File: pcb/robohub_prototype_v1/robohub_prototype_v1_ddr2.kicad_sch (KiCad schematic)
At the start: 41 parts, among them U1 ATSAMA5D27C, U31 W972GG6KB-25, U32 W972GG6KB-25

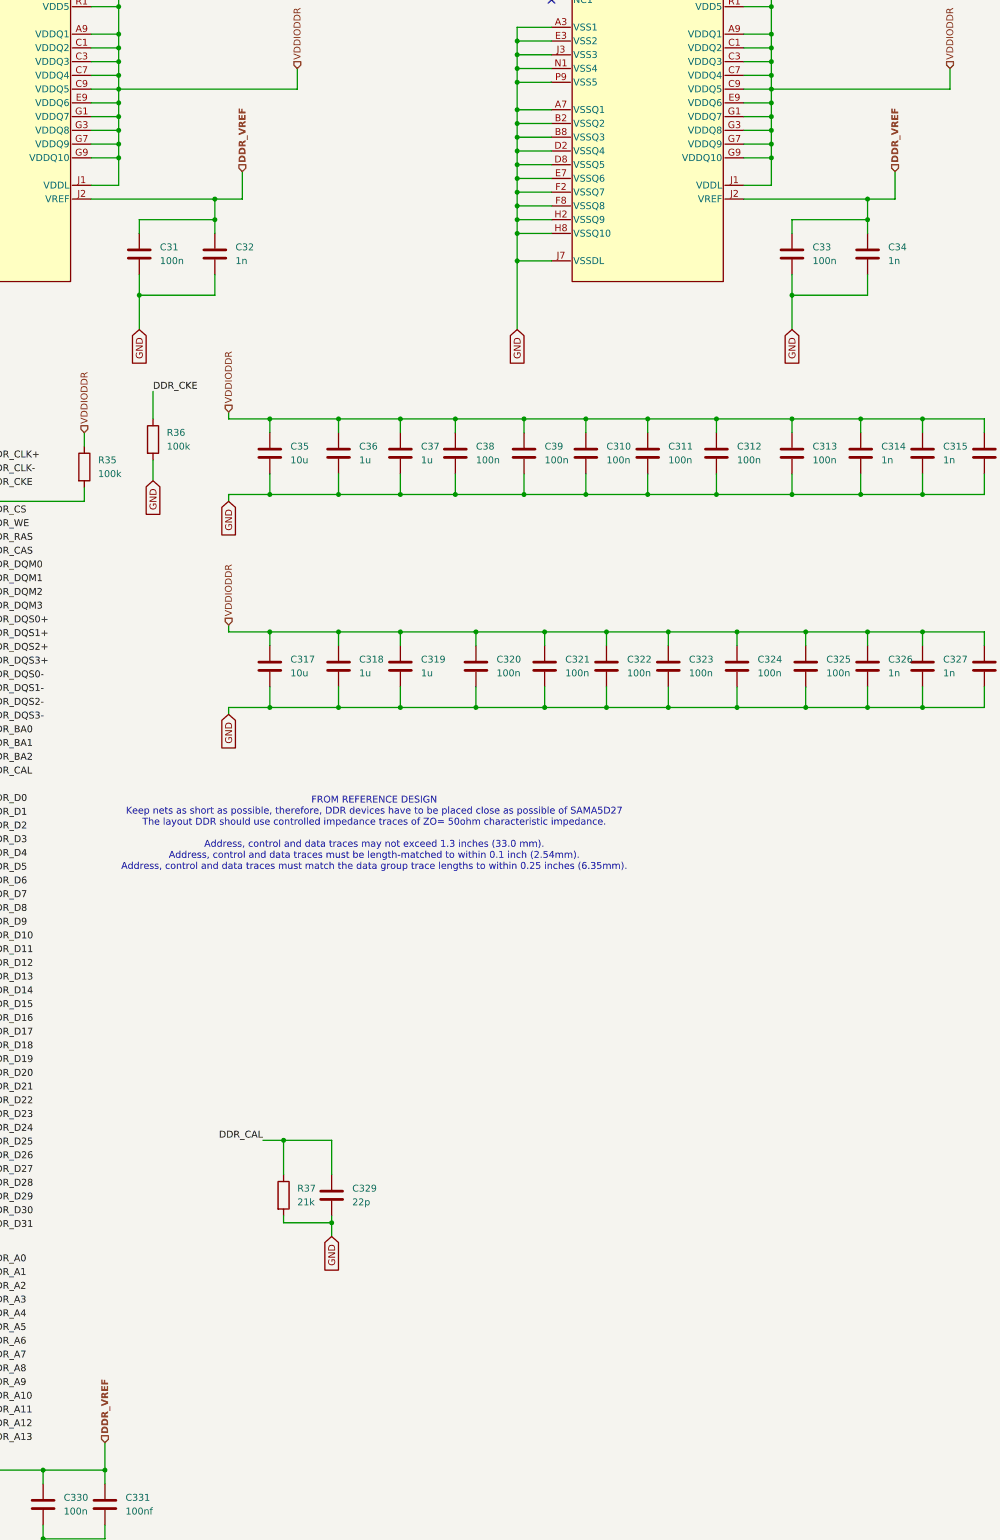
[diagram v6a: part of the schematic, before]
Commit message: Start routing ddr2
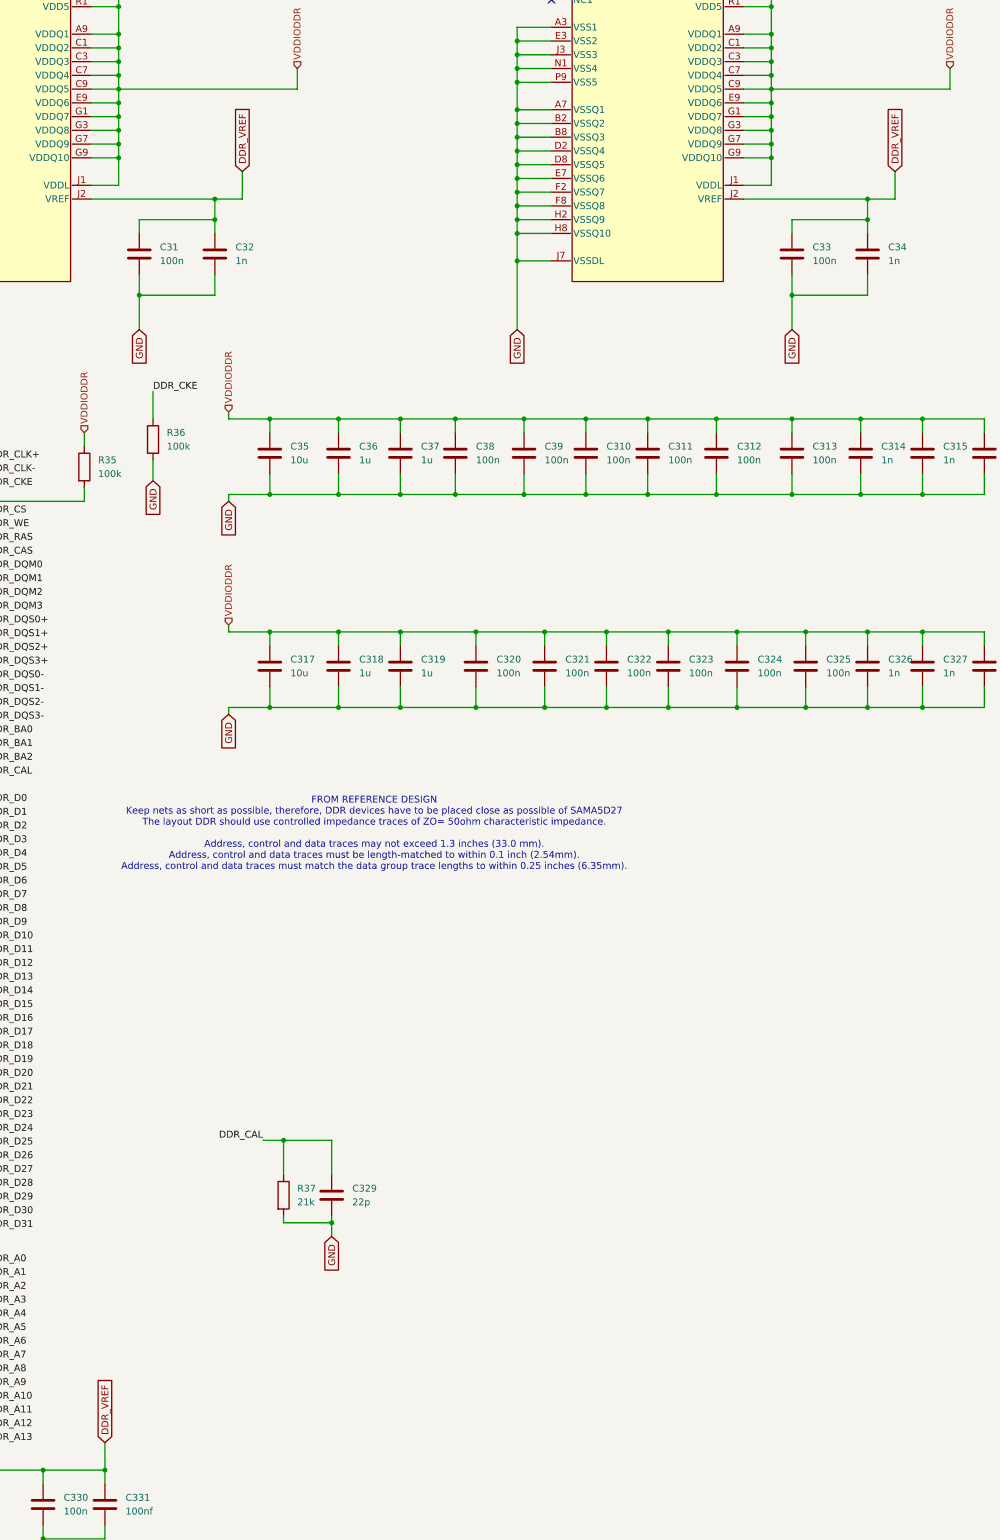
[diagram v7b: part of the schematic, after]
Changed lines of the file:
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@@
+		)
+	)
+	(global_label "DDR_VREF"
+		(shape input)
+		(at 120.65 156.21 90)
+		(fields_autoplaced yes)
+		(effects
+			(font
+				(size 1.27 1.27)
+			)
+			(justify left)
+		)
+		(property "Intersheetrefs" "${INTERSHEET_REFS}"
+			(at 120.65 143.851 90)
+			(effects
+				(font
+					(size 1.27 1.27)
+				)
+				(justify left)
+				(hide yes)
+			)
 		)
 	)
@@
 		)
 	)
+	(global_label "DDR_VREF"
+		(shape input)
+		(at 95.25 391.16 90)
+		(fields_autoplaced yes)
+		(effects
+			(font
+				(size 1.27 1.27)
+			)
+			(justify left)
+		)
+		(property "Intersheetrefs" "${INTERSHEET_REFS}"
+			(at 95.25 378.801 90)
+			(effects
+				(font
+					(size 1.27 1.27)
+				)
+				(justify left)
+				(hide yes)
+			)
+		)
+	)
 	(global_label "GND"
 		(shape input)
@@
 		)
 	)
+	(global_label "DDR_VREF"
+		(shape input)
+		(at 241.3 156.21 90)
+		(fields_autoplaced yes)
+		(effects
+			(font
+				(size 1.27 1.27)
+			)
+			(justify left)
+		)
+		(property "Intersheetrefs" "${INTERSHEET_REFS}"
+			(at 241.3 143.851 90)
+			(effects
+				(font
+					(size 1.27 1.27)
+				)
+				(justify left)
+				(hide yes)
+			)
+		)
+	)
 	(global_label "GND"
 		(shape input)
@@
 		)
 	)
-	(hierarchical_label "DDR_VREF"
-		(shape input)
-		(at 241.3 156.21 90)
-		(fields_autoplaced yes)
-		(effects
-			(font
-				(size 1.27 1.27)
-				(bold yes)
-			)
-			(justify left)
-		)
-	)
-	(hierarchical_label "DDR_VREF"
-		(shape input)
-		(at 120.65 156.21 90)
-		(fields_autoplaced yes)
-		(effects
-			(font
-				(size 1.27 1.27)
-				(bold yes)
-			)
-			(justify left)
-		)
-	)
 	(hierarchical_label "VDDIODDR"
 		(shape input)
@@
 			)
 			(justify left)
-		)
-	)
-	(hierarchical_label "DDR_VREF"
-		(shape input)
-		(at 95.25 391.16 90)
-		(fields_autoplaced yes)
-		(effects
-			(font
-				(size 1.27 1.27)
-				(bold yes)
-			)
-			(justify left)

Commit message: Update schematic for byte swap; change ddr2 layout; begin reroute of ddr2
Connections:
- net DDR_D10: now also U32.H7 (DQ2); no longer U31.D7 (DQ10)
- net DDR_D11: now also U32.H3 (DQ3); no longer U31.D3 (DQ11)
- net DDR_D12: now also U32.H1 (DQ4); no longer U31.D1 (DQ12)
- net DDR_D13: now also U32.H9 (DQ5); no longer U31.D9 (DQ13)
- net DDR_D14: now also U32.F1 (DQ6); no longer U31.B1 (DQ14)
- net DDR_D15: now also U32.F9 (DQ7); no longer U31.B9 (DQ15)
- net DDR_D16: now also U31.C8 (DQ8); no longer U32.G8 (DQ0)
- net DDR_D17: now also U31.C2 (DQ9); no longer U32.G2 (DQ1)
- net DDR_D18: now also U31.D7 (DQ10); no longer U32.H7 (DQ2)
- net DDR_D19: now also U31.D3 (DQ11); no longer U32.H3 (DQ3)
- net DDR_D20: now also U31.D1 (DQ12); no longer U32.H1 (DQ4)
- net DDR_D21: now also U31.D9 (DQ13); no longer U32.H9 (DQ5)
- net DDR_D22: now also U31.B1 (DQ14); no longer U32.F1 (DQ6)
- net DDR_D23: now also U31.B9 (DQ15); no longer U32.F9 (DQ7)
- net DDR_D8: now also U32.G8 (DQ0); no longer U31.C8 (DQ8)
- net DDR_D9: now also U32.G2 (DQ1); no longer U31.C2 (DQ9)
- net DDR_DQM1: now also U32.F3 (LDM); no longer U31.B3 (UDM)
- net DDR_DQM2: now also U31.B3 (UDM); no longer U32.F3 (LDM)
- net DDR_DQS1+: now also U32.F7 (LDQS_P); no longer U31.B7 (UDQS_P)
- net DDR_DQS1-: now also U32.E8 (NU/LDQS_N); no longer U31.A8 (NU/UDQS_N)
- net DDR_DQS2+: now also U31.B7 (UDQS_P); no longer U32.F7 (LDQS_P)
- net DDR_DQS2-: now also U31.A8 (NU/UDQS_N); no longer U32.E8 (NU/LDQS_N)
